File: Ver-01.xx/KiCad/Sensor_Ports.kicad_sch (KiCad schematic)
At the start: 28 parts

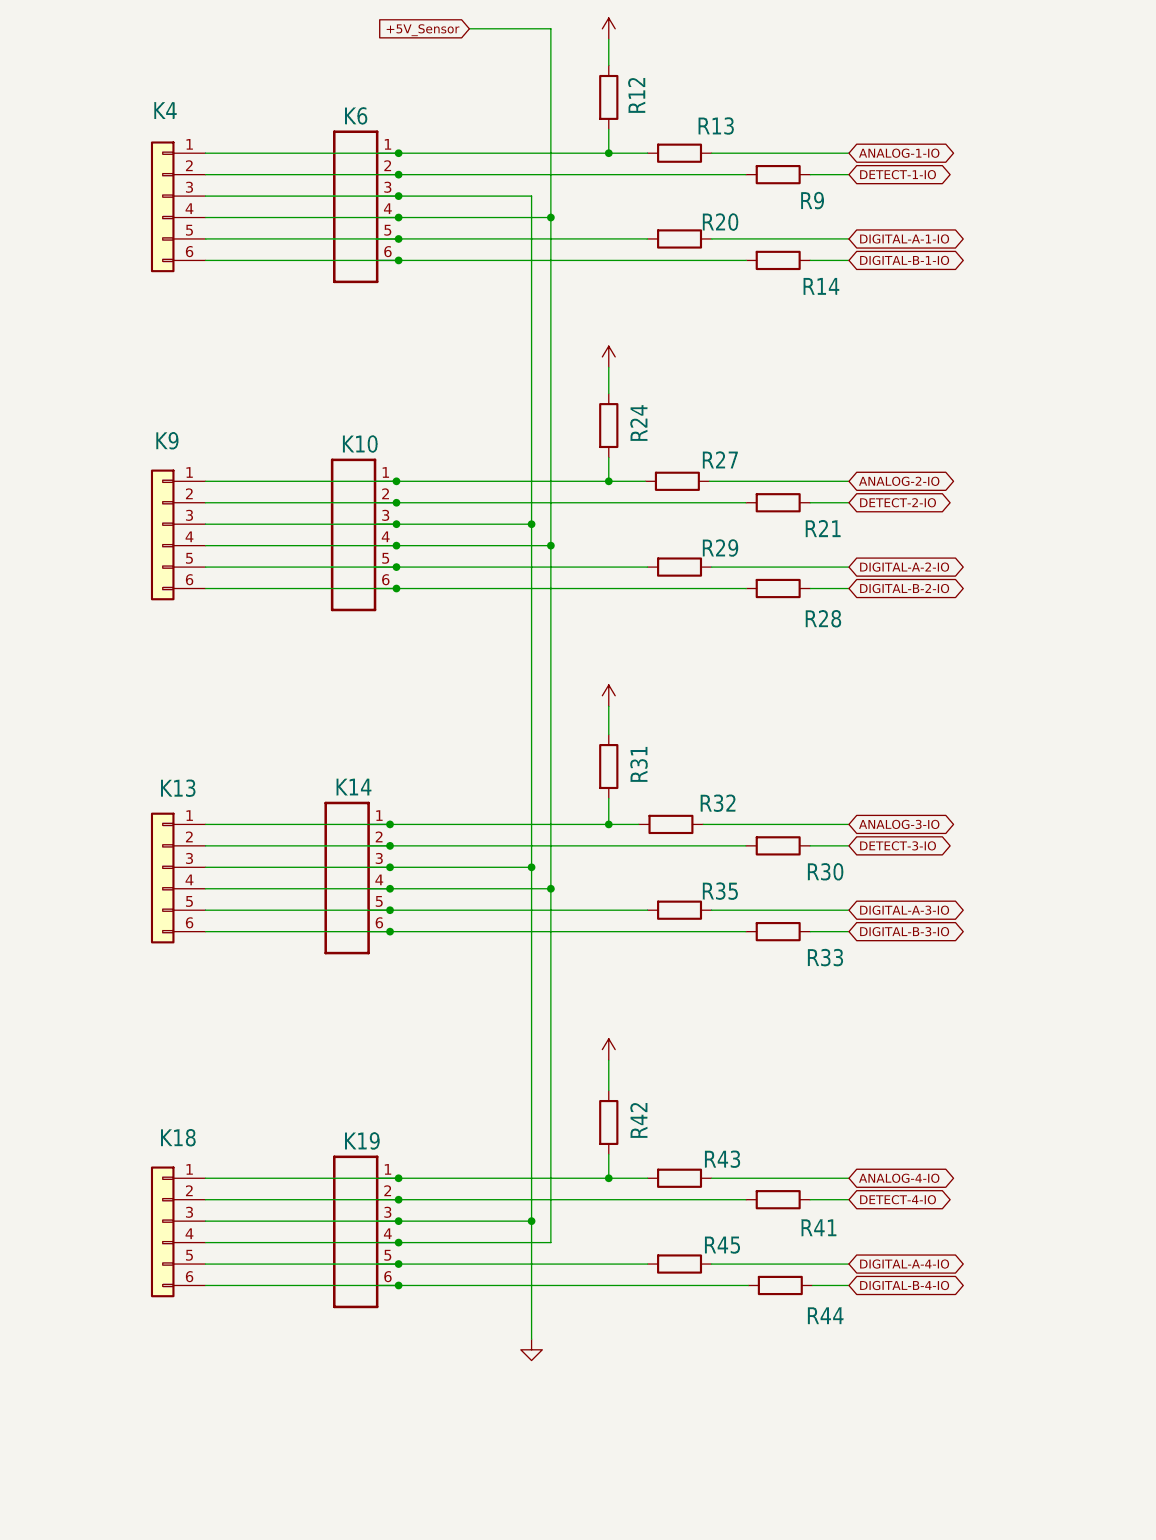
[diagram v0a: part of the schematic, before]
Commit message: Snap to grid
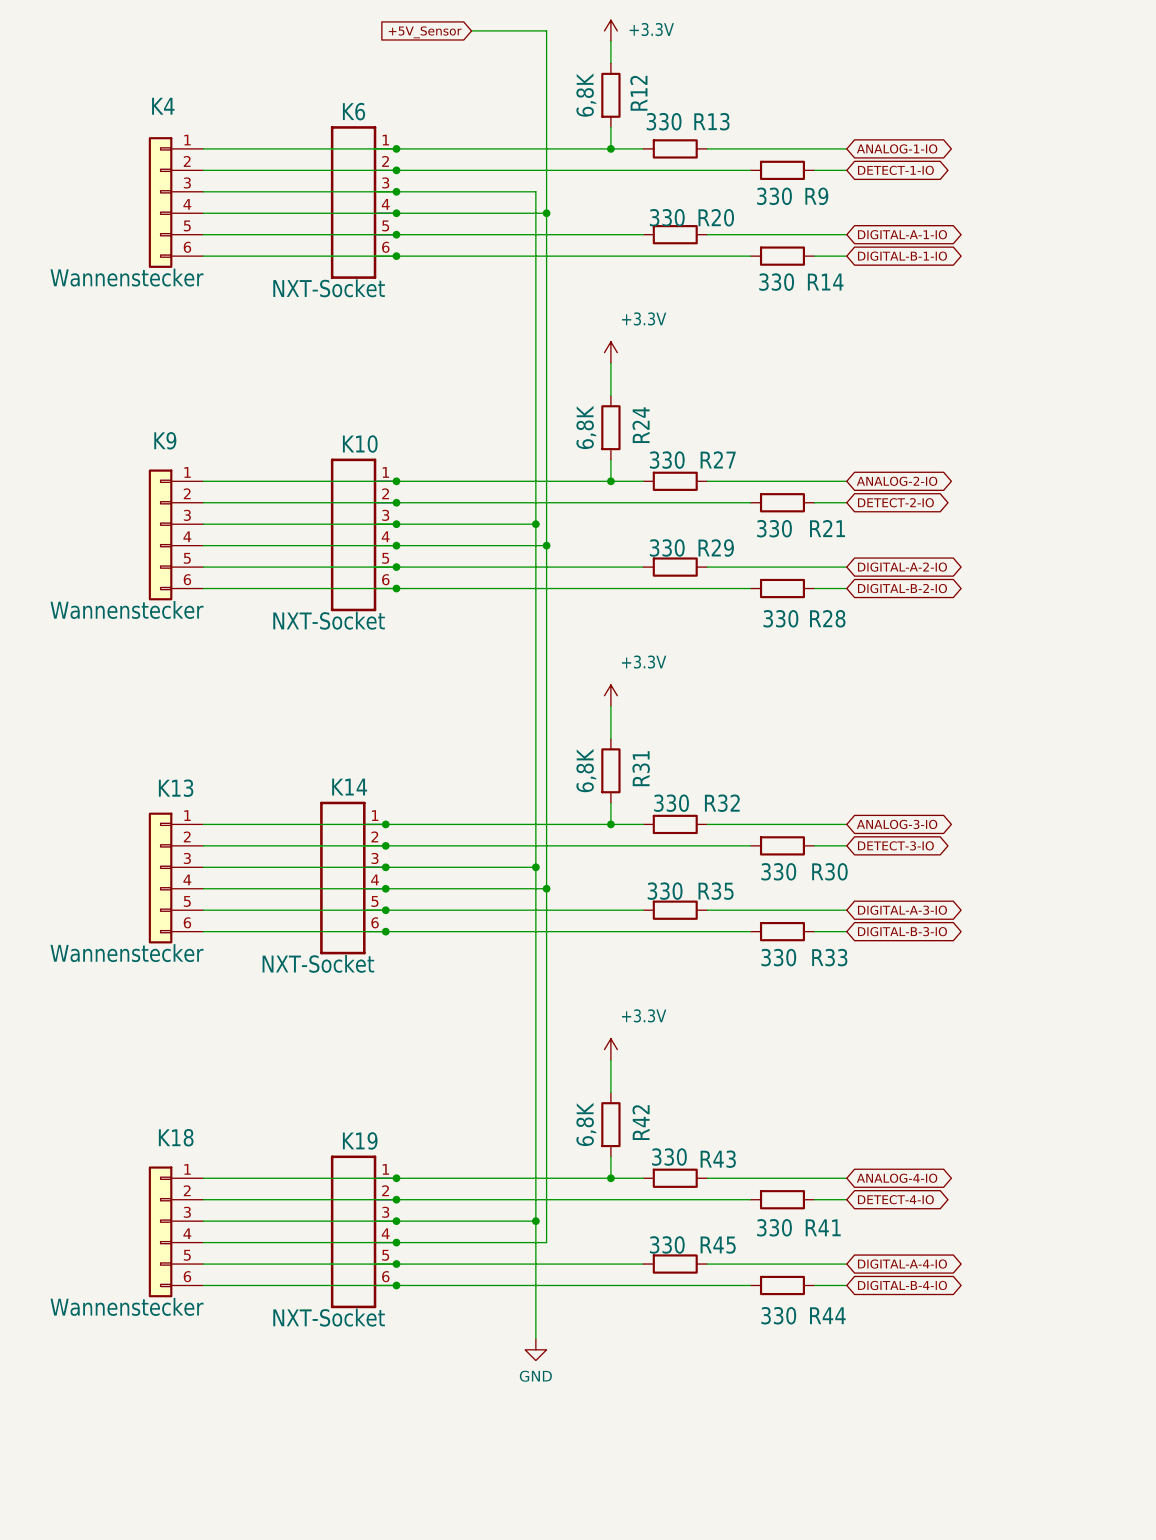
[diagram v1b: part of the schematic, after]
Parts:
- K10, K14, K19, K6: value (none) -> NXT-Socket; footprint (none) -> ORB:NXT-SOCKET
- K13, K18, K4, K9: value (none) -> Wannenstecker; footprint (none) -> ORB:IDC-Header_2x03_P2.54mm_Vertical
- R12, R24, R31, R42: value (none) -> 6,8K; footprint (none) -> Resistor_SMD:R_0603_1608Metric
- R13, R14, R20, R21, R27, R28, R29, R30, R32, R33, R35, R41, R43, R44, R45, R9: value (none) -> 330; footprint (none) -> Resistor_SMD:R_0603_1608Metric
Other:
- moved on the sheet: K14, K4, K6, R13, R14, R20, R21, R28, R29, R30, R31, R32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
